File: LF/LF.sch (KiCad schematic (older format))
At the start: 7 parts, among them J1 SpeakON_NL4, J2 SpeakON_NL4

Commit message: changes from Trello
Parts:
- added J3: Conn_01x02_Female, RES:Faston_DUAL_01x02_P5.08mm_D5.08mm, symbol Connector:Conn_01x02_Female
- C1: footprint (none) -> RES:cps22
- L1: footprint (none) -> RES:inductor_D40mm
- L2: footprint (none) -> RES:inductor_P28mm
- R1, R2: footprint (none) -> RES:ptc_7.2mm_larger
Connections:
- wire segments 32 -> 36
- no-connect marks 1 -> 0
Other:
- note removed: "+"
- note removed: "-"
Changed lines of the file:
@@
 F 0 "R1" V 6043 4100 50  0000 C CNN
 F 1 "100mΩ" V 6134 4100 50  0000 C CNN
-F 2 "" V 6180 4100 50  0001 C CNN
+F 2 "RES:ptc_7.2mm_larger" V 6180 4100 50  0001 C CNN
 F 3 "~" H 6250 4100 50  0001 C CNN
 	1    6250 4100
@@
 F 0 "R2" V 6043 4450 50  0000 C CNN
 F 1 "100mΩ" V 6134 4450 50  0000 C CNN
-F 2 "" V 6180 4450 50  0001 C CNN
+F 2 "RES:ptc_7.2mm_larger" V 6180 4450 50  0001 C CNN
 F 3 "~" H 6250 4450 50  0001 C CNN
 	1    6250 4450
@@
 F 0 "L1" V 6719 4100 50  0000 C CNN
 F 1 "890uH" V 6810 4100 50  0000 C CNN
-F 2 "" H 6900 4100 50  0001 C CNN
+F 2 "RES:inductor_D40mm" H 6900 4100 50  0001 C CNN
 F 3 "~" H 6900 4100 50  0001 C CNN
 	1    6900 4100
@@
 F 0 "L2" V 7319 4100 50  0000 C CNN
 F 1 "250uH" V 7410 4100 50  0000 C CNN
-F 2 "" H 7500 4100 50  0001 C CNN
+F 2 "RES:inductor_P28mm" H 7500 4100 50  0001 C CNN
 F 3 "~" H 7500 4100 50  0001 C CNN
 	1    7500 4100
@@
 F 0 "C1" H 7315 4446 50  0000 L CNN
 F 1 "22uF" H 7315 4355 50  0000 L CNN
-F 2 "" H 7238 4250 50  0001 C CNN
+F 2 "RES:cps22" H 7238 4250 50  0001 C CNN
 F 3 "~" H 7200 4400 50  0001 C CNN
 	1    7200 4400
@@
 $EndComp
 Wire Wire Line
-	6100 4450 5850 4450
+	6100 4450 5900 4450
 Wire Wire Line
-	5850 4450 5850 4100
-Connection ~ 5850 4100
+	5900 4450 5900 4100
+Connection ~ 5900 4100
 Wire Wire Line
-	5850 4100 6100 4100
+	5900 4100 6100 4100
 Wire Wire Line
 	6400 4450 6600 4450
@@
 Connection ~ 7200 4100
 Wire Wire Line
-	7200 4550 7200 4650
+	7200 4550 7200 4700
 Wire Wire Line
 	7800 4100 7650 4100
 Wire Wire Line
-	7800 4650 7200 4650
-Connection ~ 7200 4650
+	7800 4700 7200 4700
+Connection ~ 7200 4700
 $Comp
 L Connector:SpeakON_NL4 J2
@@
 	5300 3350 5300 4100
 Wire Wire Line
-	5300 4100 5850 4100
+	5300 4100 5900 4100
 Wire Wire Line
-	4900 4650 4900 3700
+	4900 4700 4900 3700
 Wire Wire Line
-	4900 4650 7200 4650
+	4900 4700 7200 4700
 Connection ~ 4900 3700
 Wire Wire Line
-	4450 2700 4450 3350
+	4500 2700 4500 3350
 Wire Wire Line
-	4450 3350 4600 3350
+	4500 3350 4600 3350
 Wire Wire Line
 	3500 2700 3500 3350
@@
 	3500 3350 3600 3350
 Wire Wire Line
-	3500 2700 4450 2700
+	3500 2700 4500 2700
 Connection ~ 5300 4100
 Wire Wire Line
@@
 Wire Wire Line
 	4300 4100 5300 4100
-NoConn ~ 7800 4100
-Text Notes 7950 4150 0    50   ~ 0
-+
-Text Notes 7950 4650 0    50   ~ 0
--
+$Comp
+L Connector:Conn_01x02_Female J3
+U 1 1 60A52CA7
+P 8100 4350
+F 0 "J3" H 8128 4326 50  0000 L CNN
+F 1 "Conn_01x02_Female" H 8128 4235 50  0000 L CNN
+F 2 "RES:Faston_DUAL_01x02_P5.08mm_D5.08mm" H 8100 4350 50  0001 C CNN
+F 3 "~" H 8100 4350 50  0001 C CNN
+	1    8100 4350
+	1    0    0    -1
+$EndComp
+Wire Wire Line
+	7900 4450 7800 4450
+Wire Wire Line
+	7800 4450 7800 4700
+Wire Wire Line
+	7900 4350 7800 4350
+Wire Wire Line
+	7800 4350 7800 4100
 $EndSCHEMATC

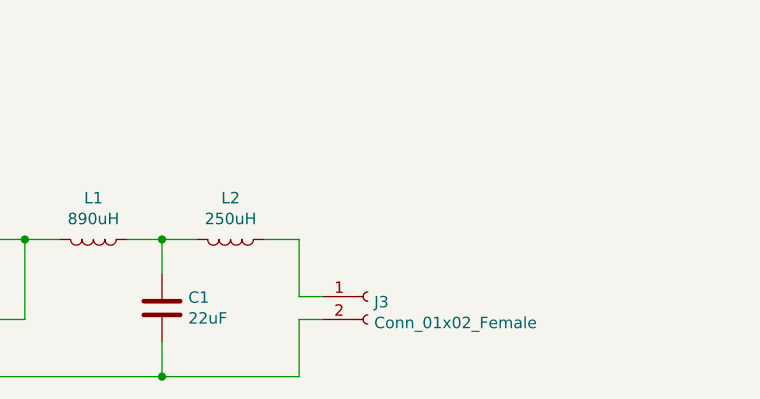
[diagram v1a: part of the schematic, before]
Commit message: added parallel board
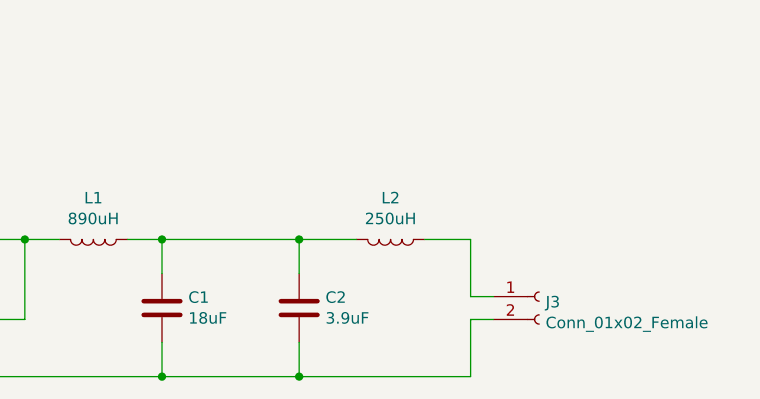
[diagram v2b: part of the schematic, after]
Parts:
- added C2: 3.9uF, RES:cps22, symbol Device:C
- C1: value 22uF -> 18uF
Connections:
- net at C1.1, L1.1, L2.2: now also C2.1
- net at C1.2, J1.2-, J2.2-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: now also C2.2
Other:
- moved on the sheet: J3, L2
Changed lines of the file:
@@
 L Device:L L2
 U 1 1 60A12320
-P 7500 4100
-F 0 "L2" V 7319 4100 50  0000 C CNN
-F 1 "250uH" V 7410 4100 50  0000 C CNN
-F 2 "RES:inductor_P28mm" H 7500 4100 50  0001 C CNN
-F 3 "~" H 7500 4100 50  0001 C CNN
-	1    7500 4100
+P 8200 4100
+F 0 "L2" V 8019 4100 50  0000 C CNN
+F 1 "250uH" V 8110 4100 50  0000 C CNN
+F 2 "RES:inductor_P28mm" H 8200 4100 50  0001 C CNN
+F 3 "~" H 8200 4100 50  0001 C CNN
+	1    8200 4100
 	0    1    1    0
 $EndComp
@@
 P 7200 4400
 F 0 "C1" H 7315 4446 50  0000 L CNN
-F 1 "22uF" H 7315 4355 50  0000 L CNN
+F 1 "18uF" H 7315 4355 50  0000 L CNN
 F 2 "RES:cps22" H 7238 4250 50  0001 C CNN
 F 3 "~" H 7200 4400 50  0001 C CNN
@@
 Wire Wire Line
 	7200 4100 7050 4100
-Wire Wire Line
-	7350 4100 7200 4100
 Connection ~ 7200 4100
 Wire Wire Line
 	7200 4550 7200 4700
 Wire Wire Line
-	7800 4100 7650 4100
-Wire Wire Line
-	7800 4700 7200 4700
-Connection ~ 7200 4700
+	8550 4100 8350 4100
 $Comp
 L Connector:SpeakON_NL4 J2
@@
 L Connector:Conn_01x02_Female J3
 U 1 1 60A52CA7
-P 8100 4350
-F 0 "J3" H 8128 4326 50  0000 L CNN
-F 1 "Conn_01x02_Female" H 8128 4235 50  0000 L CNN
-F 2 "RES:Faston_DUAL_01x02_P5.08mm_D5.08mm" H 8100 4350 50  0001 C CNN
-F 3 "~" H 8100 4350 50  0001 C CNN
-	1    8100 4350
+P 8850 4350
+F 0 "J3" H 8878 4326 50  0000 L CNN
+F 1 "Conn_01x02_Female" H 8878 4235 50  0000 L CNN
+F 2 "RES:Faston_DUAL_01x02_P5.08mm_D5.08mm" H 8850 4350 50  0001 C CNN
+F 3 "~" H 8850 4350 50  0001 C CNN
+	1    8850 4350
 	1    0    0    -1
 $EndComp
 Wire Wire Line
-	7900 4450 7800 4450
+	8650 4450 8550 4450
 Wire Wire Line
-	7800 4450 7800 4700
+	8550 4450 8550 4700
 Wire Wire Line
-	7900 4350 7800 4350
+	8650 4350 8550 4350
 Wire Wire Line
-	7800 4350 7800 4100
+	8550 4350 8550 4100
+$Comp
+L Device:C C2
+U 1 1 60D66DF1
+P 7800 4400
+F 0 "C2" H 7915 4446 50  0000 L CNN
+F 1 "3.9uF" H 7915 4355 50  0000 L CNN
+F 2 "RES:cps22" H 7838 4250 50  0001 C CNN
+F 3 "~" H 7800 4400 50  0001 C CNN
+	1    7800 4400
+	1    0    0    -1
+$EndComp
+Wire Wire Line
+	7800 4550 7800 4700
+Wire Wire Line
+	7800 4700 7200 4700
+Connection ~ 7200 4700
+Wire Wire Line
+	7800 4700 8550 4700
+Connection ~ 7800 4700
+Wire Wire Line
+	7800 4250 7800 4100
+Wire Wire Line
+	7200 4100 7800 4100
+Wire Wire Line
+	7800 4100 8050 4100
+Connection ~ 7800 4100
 $EndSCHEMATC
